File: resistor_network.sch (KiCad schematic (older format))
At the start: 0 parts

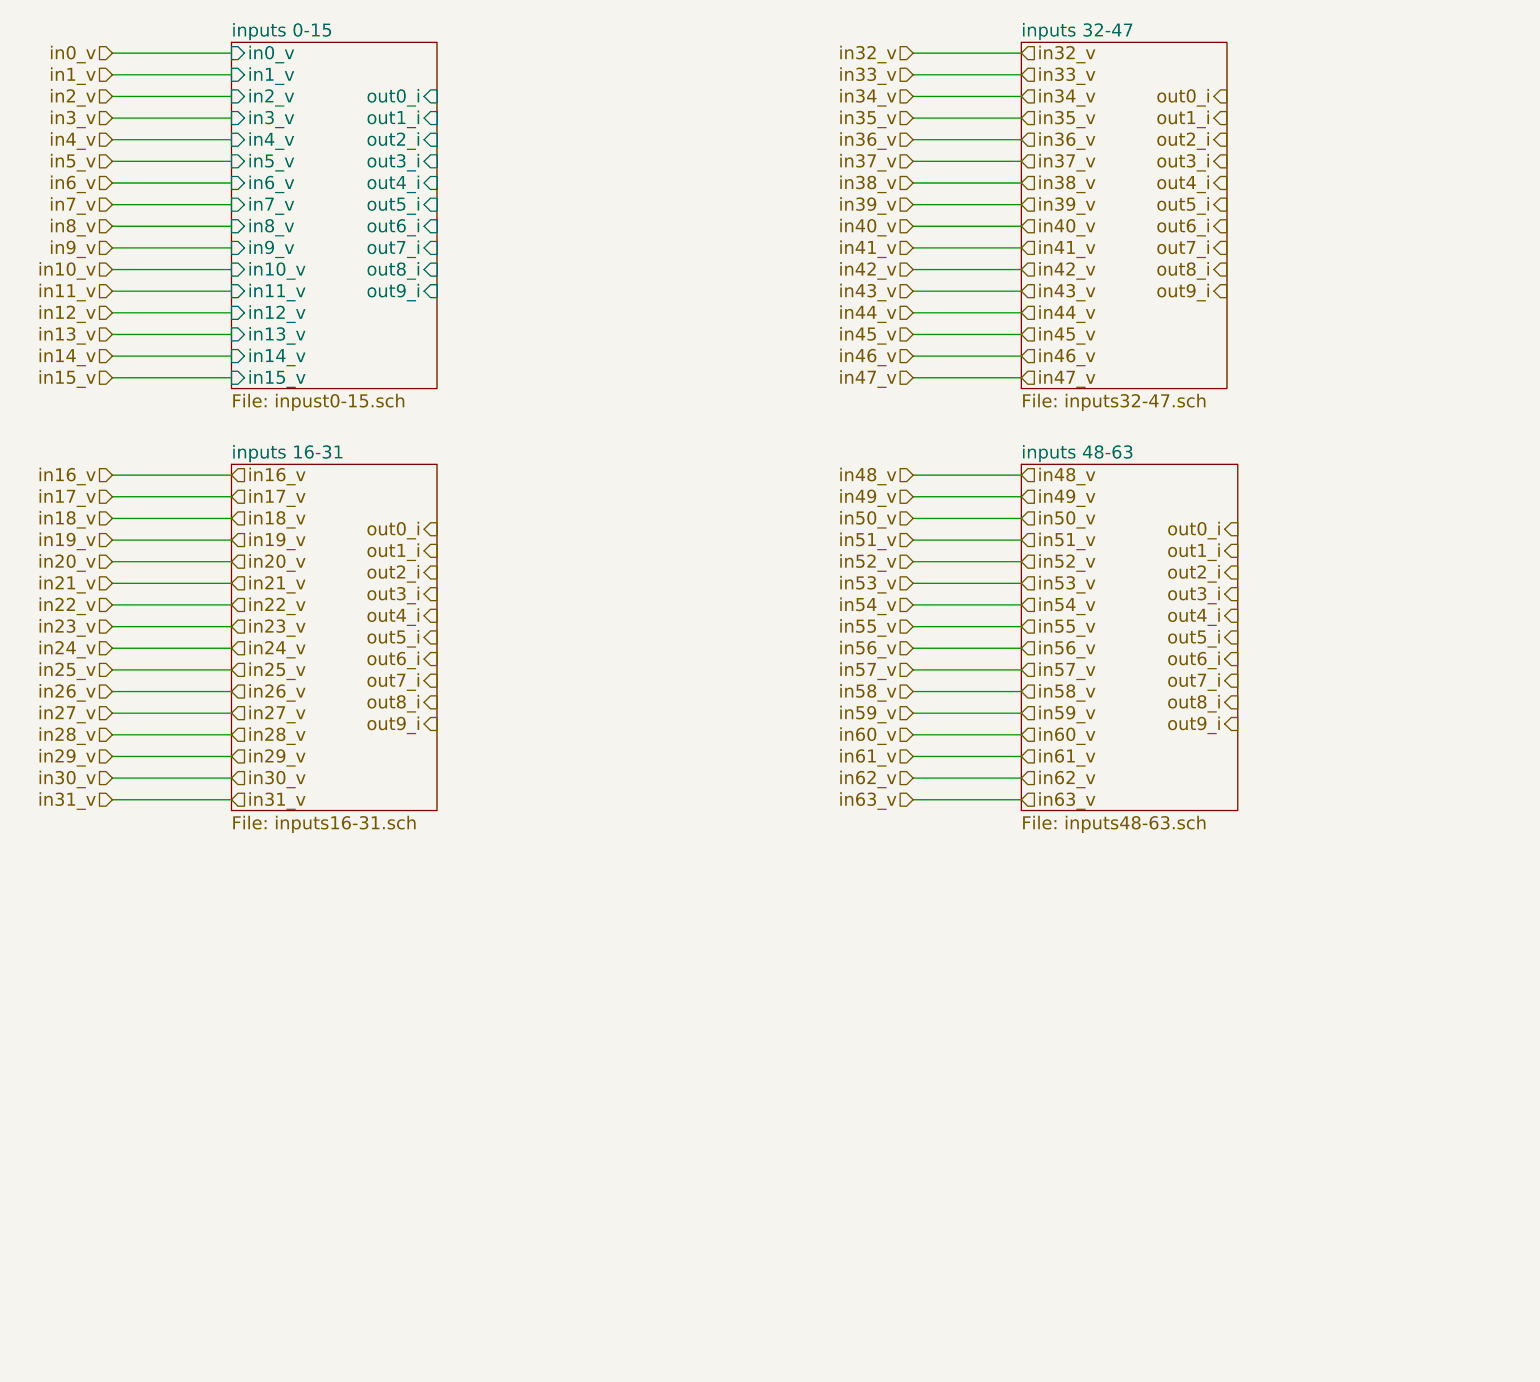
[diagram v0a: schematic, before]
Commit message: added output wires
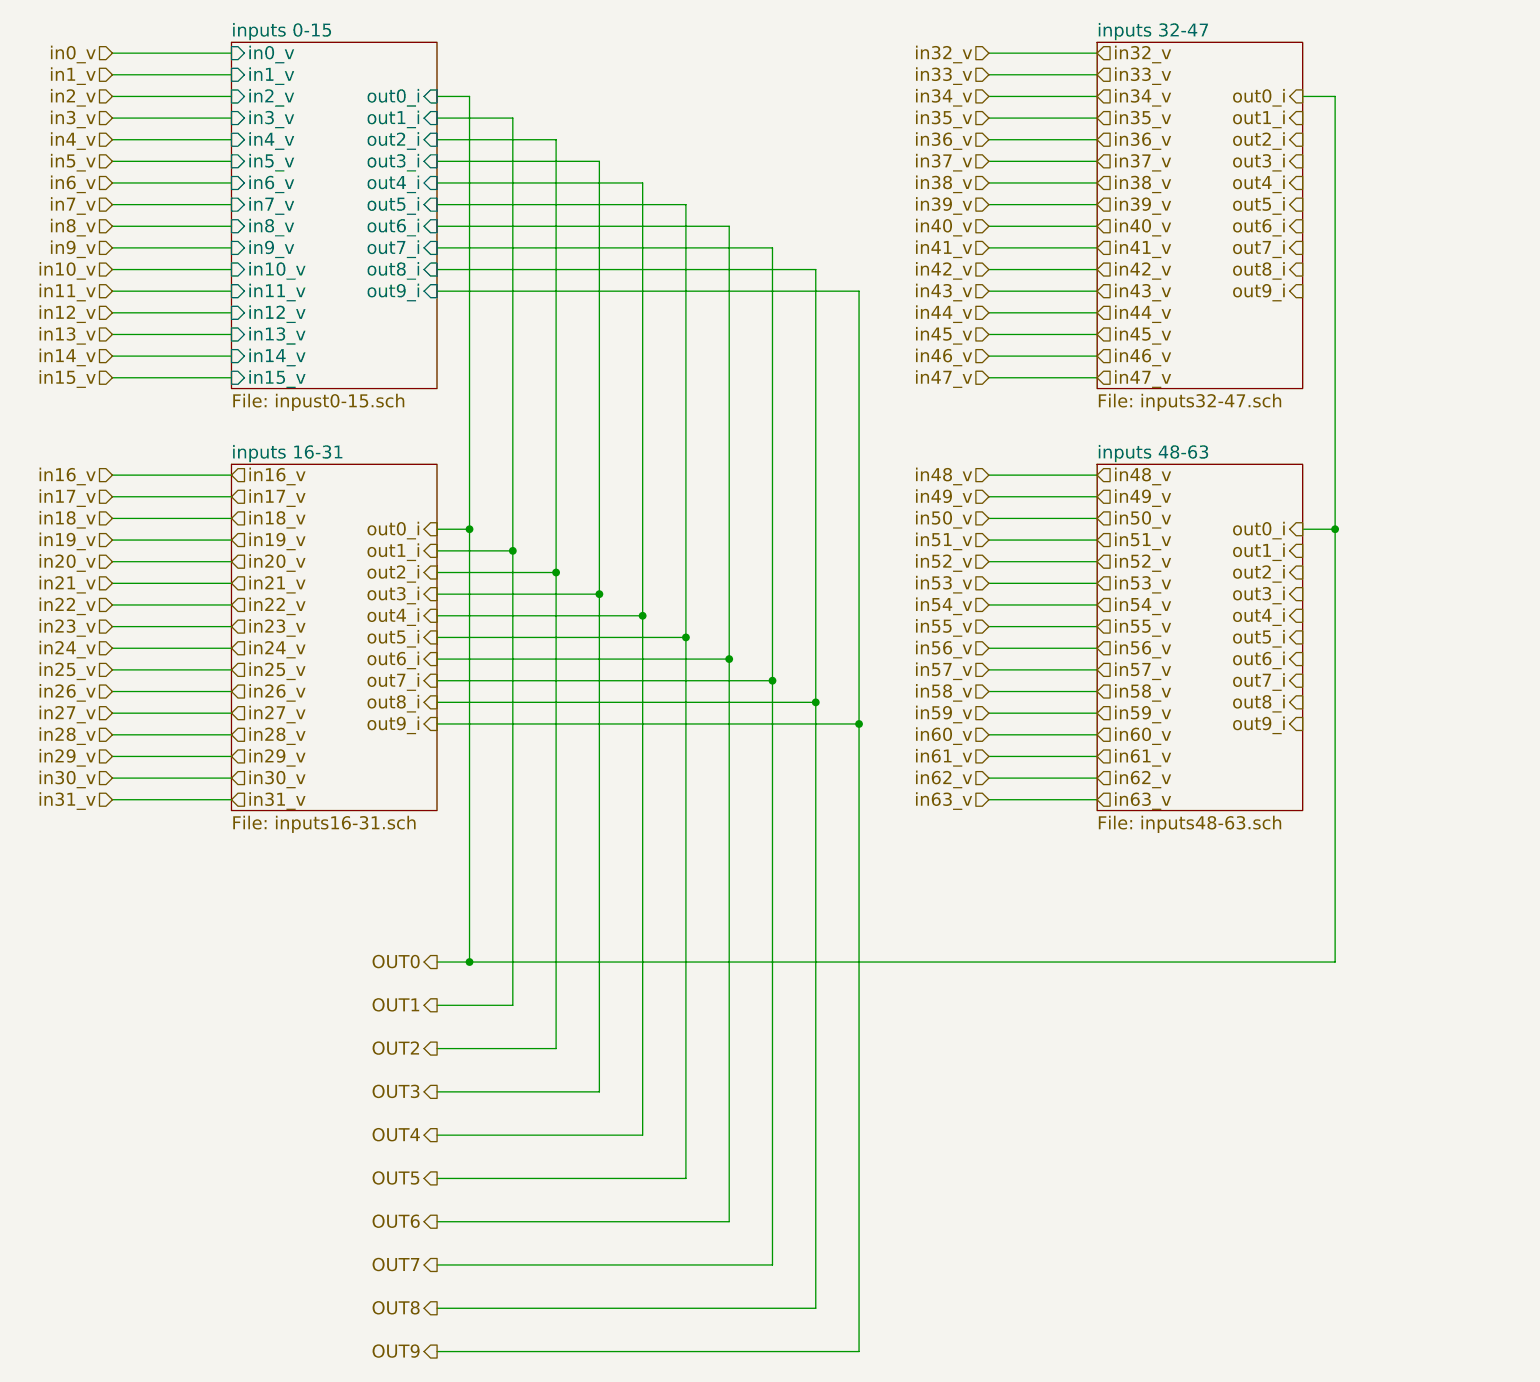
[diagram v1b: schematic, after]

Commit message: Added some wires
Added some wires, placed some terminals. Just a little bit of work.
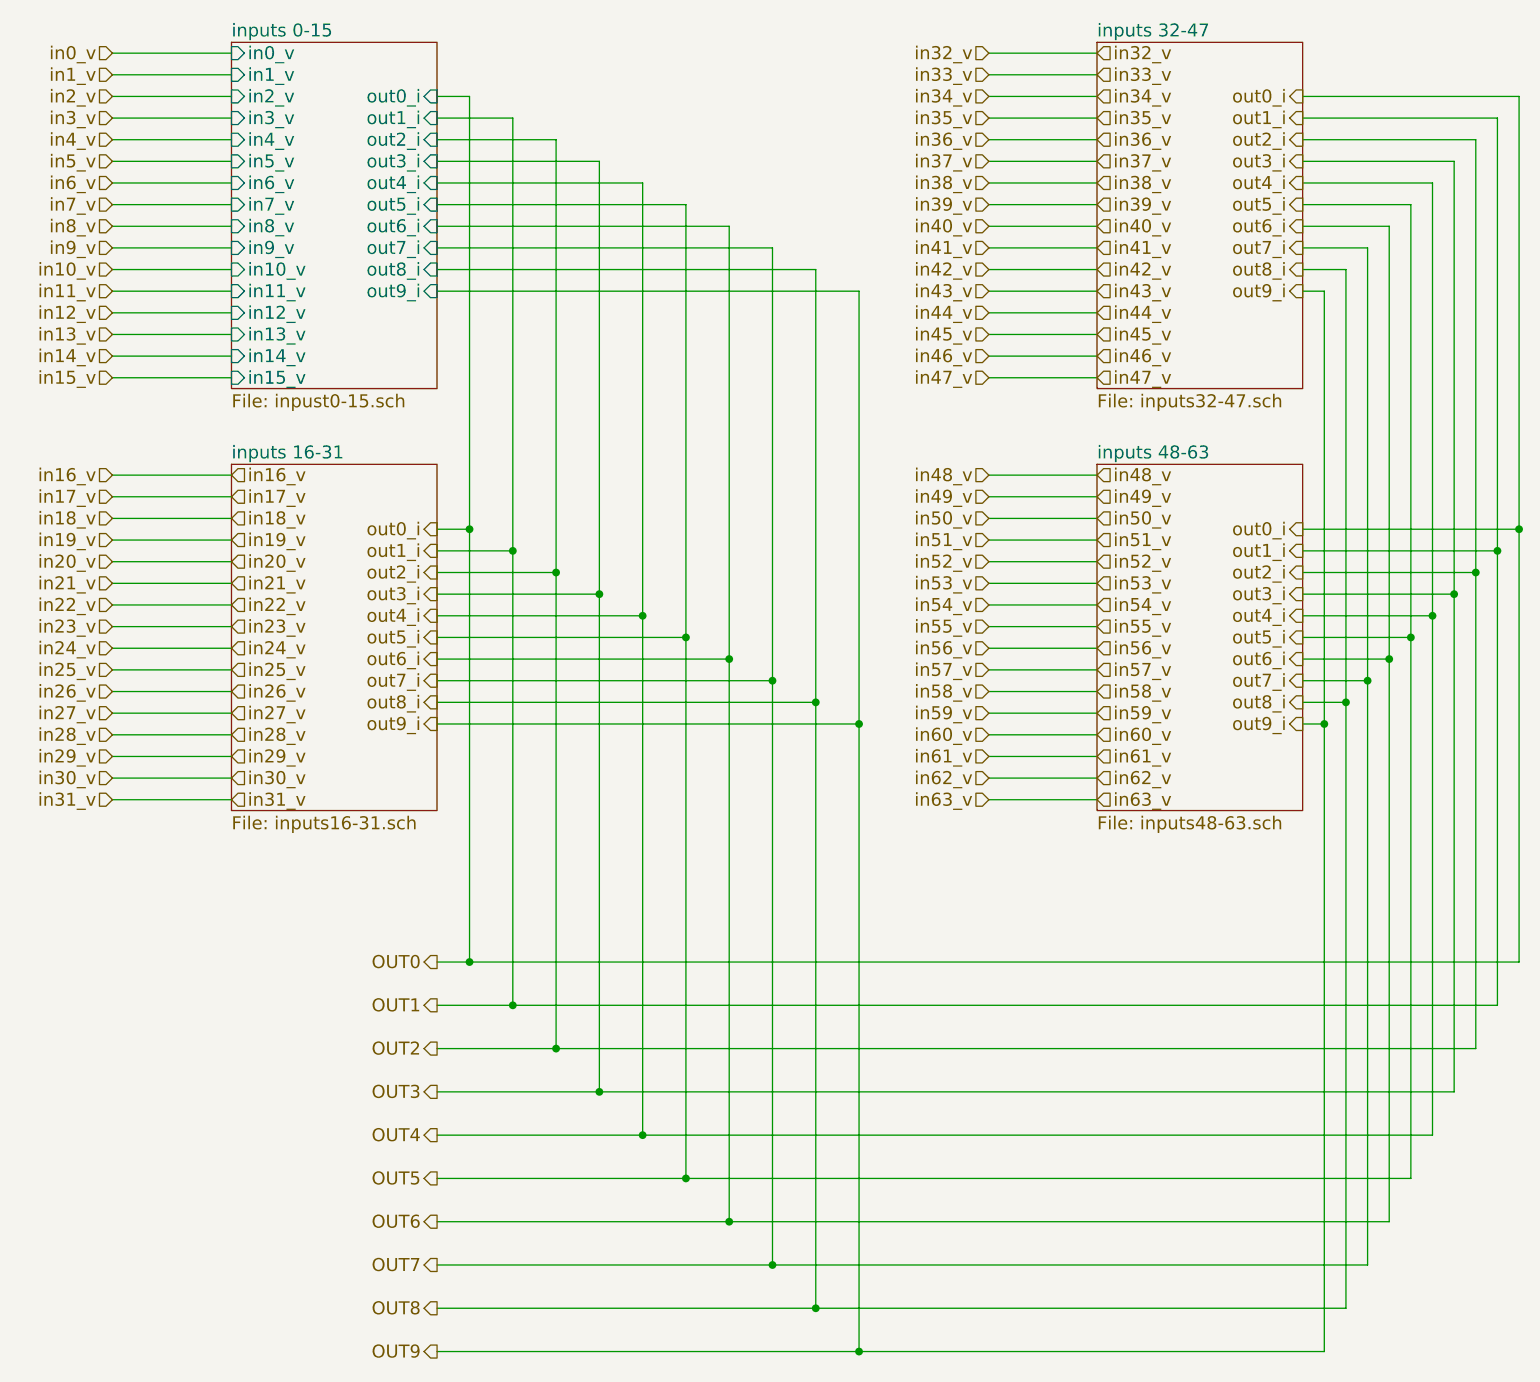
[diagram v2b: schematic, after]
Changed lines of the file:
@@
 	4900 2100 4900 6900
 Wire Wire Line
-	5100 7100 5100 2200
+	5100 2200 5100 7100
 Connection ~ 3300 3300
 Connection ~ 3500 3400
@@
 Connection ~ 5100 4200
 Wire Wire Line
-	7150 1300 7300 1300
+	8050 5500 3150 5500
 Wire Wire Line
-	7300 3300 7150 3300
-Connection ~ 7300 3300
+	7950 5700 3150 5700
 Wire Wire Line
-	7300 1300 7300 5300
+	7850 5900 3150 5900
 Wire Wire Line
-	7300 5300 3150 5300
+	7750 6100 3150 6100
 Wire Wire Line
-	3500 5500 3150 5500
+	7650 6300 3150 6300
 Wire Wire Line
-	3700 5700 3150 5700
+	7550 6500 3150 6500
 Wire Wire Line
-	3900 5900 3150 5900
-Wire Wire Line
-	4100 6100 3150 6100
-Wire Wire Line
-	4300 6300 3150 6300
-Wire Wire Line
-	4500 6500 3150 6500
-Wire Wire Line
-	4700 6700 3150 6700
-Wire Wire Line
-	4900 6900 3150 6900
-Wire Wire Line
-	3150 7100 5100 7100
+	7450 6700 3150 6700
 Connection ~ 3300 5300
 Text HLabel 3150 5500 0    60   Output ~ 0
@@
 Text HLabel 3150 7100 0    60   Output ~ 0
 OUT9
+Connection ~ 5100 7100
+Connection ~ 4900 6900
+Wire Wire Line
+	7150 4200 7250 4200
+Wire Wire Line
+	7250 2200 7250 7100
+Connection ~ 7250 4200
+Wire Wire Line
+	7150 2200 7250 2200
+Wire Wire Line
+	7150 2100 7350 2100
+Wire Wire Line
+	7350 2100 7350 6900
+Wire Wire Line
+	7350 4100 7150 4100
+Wire Wire Line
+	7150 2000 7450 2000
+Wire Wire Line
+	7450 2000 7450 6700
+Wire Wire Line
+	7450 4000 7150 4000
+Wire Wire Line
+	7150 1900 7550 1900
+Wire Wire Line
+	7550 1900 7550 6500
+Wire Wire Line
+	7550 3900 7150 3900
+Wire Wire Line
+	7150 1800 7650 1800
+Wire Wire Line
+	7650 1800 7650 6300
+Wire Wire Line
+	7650 3800 7150 3800
+Wire Wire Line
+	7150 1700 7750 1700
+Wire Wire Line
+	7750 1700 7750 6100
+Wire Wire Line
+	7750 3700 7150 3700
+Wire Wire Line
+	7150 1600 7850 1600
+Wire Wire Line
+	7850 1600 7850 5900
+Wire Wire Line
+	7850 3600 7150 3600
+Wire Wire Line
+	7150 3500 7950 3500
+Wire Wire Line
+	7950 1500 7950 5700
+Wire Wire Line
+	7950 1500 7150 1500
+Wire Wire Line
+	7150 1400 8050 1400
+Wire Wire Line
+	8050 1400 8050 5500
+Wire Wire Line
+	8050 3400 7150 3400
+Wire Wire Line
+	7150 1300 8150 1300
+Wire Wire Line
+	8150 1300 8150 5300
+Wire Wire Line
+	8150 3300 7150 3300
+Wire Wire Line
+	7250 7100 3150 7100
+Wire Wire Line
+	7350 6900 3150 6900
+Connection ~ 7350 4100
+Connection ~ 7450 4000
+Connection ~ 4700 6700
+Connection ~ 7550 3900
+Connection ~ 4500 6500
+Connection ~ 7650 3800
+Connection ~ 4300 6300
+Connection ~ 7750 3700
+Connection ~ 4100 6100
+Connection ~ 7850 3600
+Connection ~ 3900 5900
+Connection ~ 7950 3500
+Connection ~ 3700 5700
+Connection ~ 8050 3400
+Connection ~ 3500 5500
+Wire Wire Line
+	8150 5300 3150 5300
+Connection ~ 8150 3300
 $EndSCHEMATC

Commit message: fixed resistor schematic errors
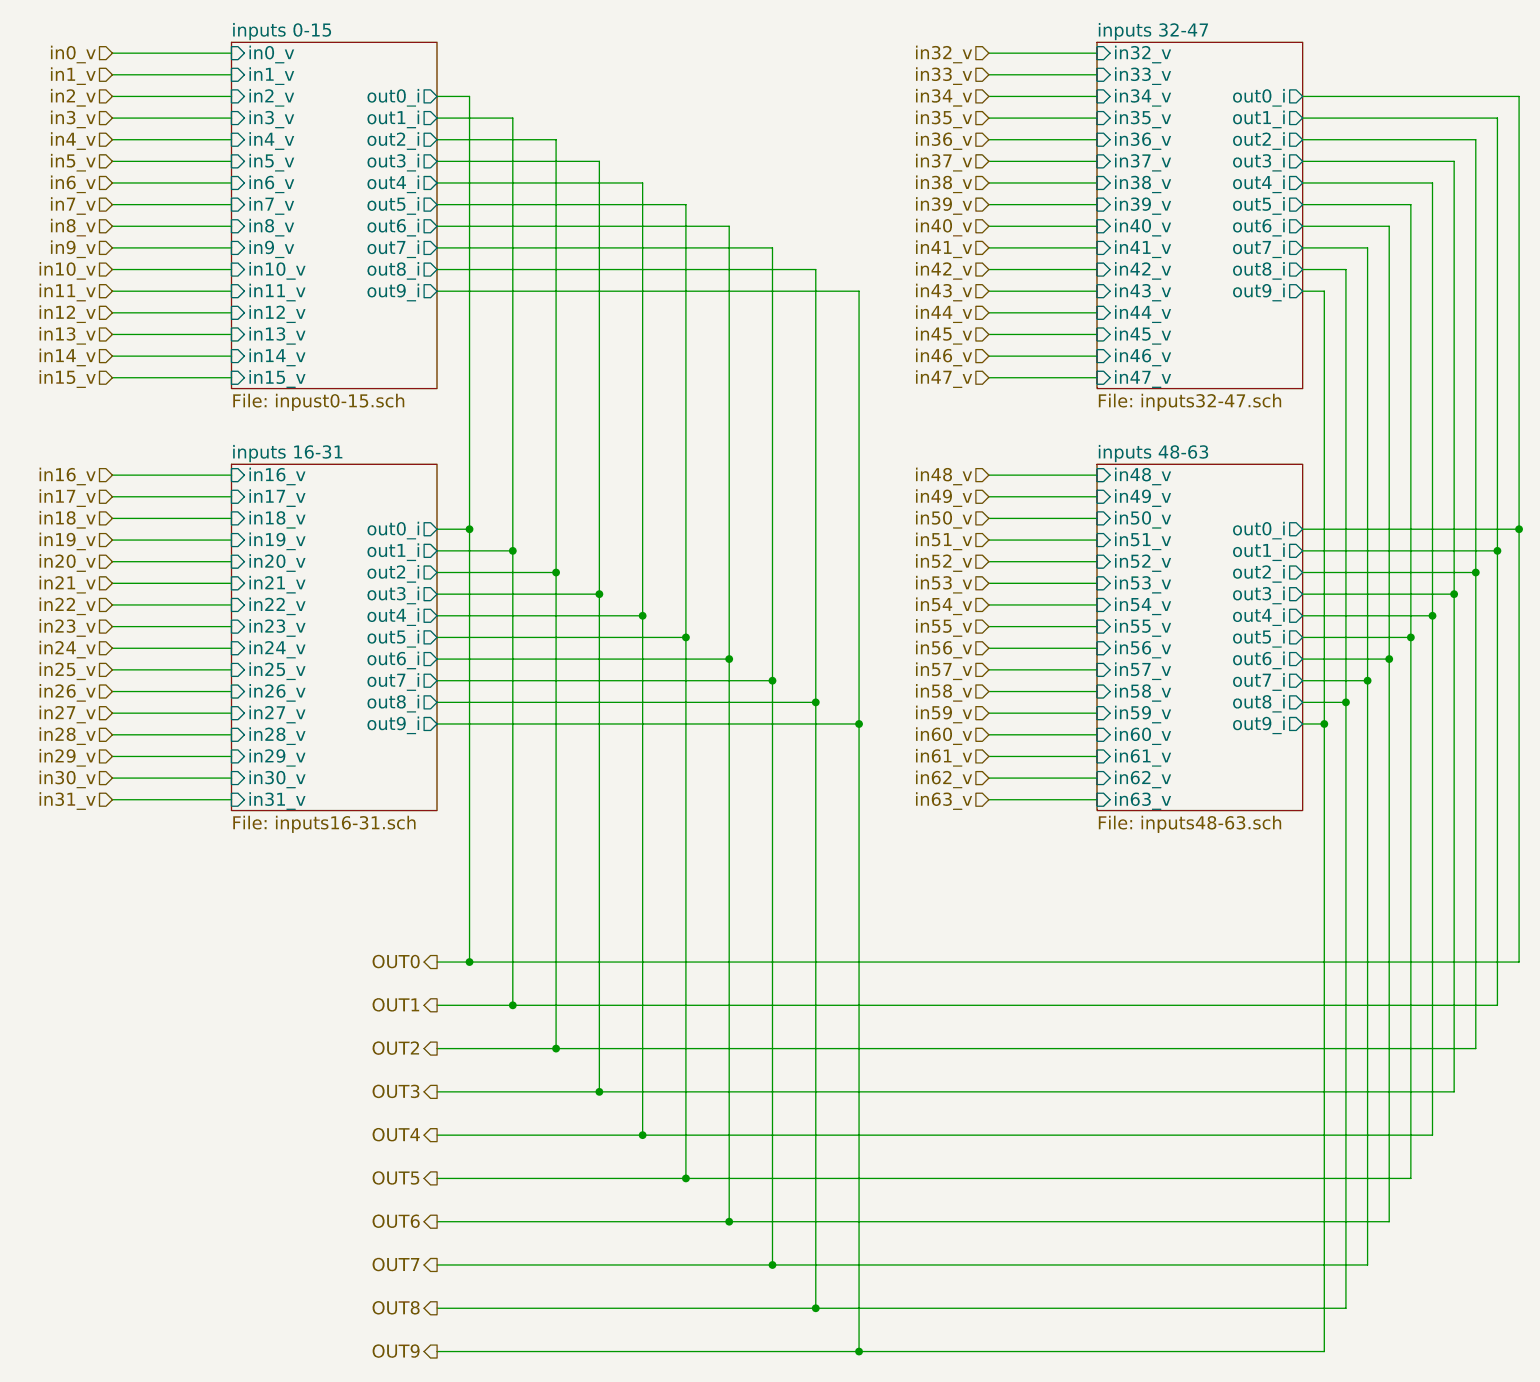
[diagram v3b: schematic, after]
